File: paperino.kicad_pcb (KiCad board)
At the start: 2 copper layers, 25.4 x 22 mm, 21 parts, among them P1 CONN_01X06, P2 CONN_01X06, P3 CONN_01X06, P4 CONN_01X06, Q1 PMOS, Q2 NMOS, U1 BMA250E, X1 XF2M-2615-1A, X2 XF2B-4545-1A

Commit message: started layout
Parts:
- moved C3 1.25 mm to (140.7, 98.3)
- moved D1 1.19 mm to (140.3, 100.3), turned to 0 degrees
- moved C7 0.67 mm to (131.3, 95.4)
- moved C6 0.58 mm to (140.2, 95.3)
- moved C5 0.58 mm to (141.9, 95.3)
- moved C2 0.29 mm to (137.9, 97.7)
- moved C9 0.26 mm to (129.1, 95.4)
- moved C8 0.20 mm to (135.9, 94.3)
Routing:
- net /GDR_N: track 2.31 -> 22.1 mm, vias 0 -> 2
- net /INT1: track 0.00 -> 19.5 mm, vias 0 -> 1
- net /INT2: track 0.00 -> 19.1 mm, vias 0 -> 1
- net /VGH: track 4.98 -> 22.7 mm
- net /SPI_CLK: track 2.35 -> 19.7 mm, vias 0 -> 1
- net /SPI_MOSI: track 2.35 -> 18.3 mm, vias 0 -> 1
- net /SPI_CS2: track 0.00 -> 15.8 mm
- net /SPI_MISO: track 2.58 -> 18.3 mm, vias 0 -> 1
- net +3V3: track 12.3 -> 28.0 mm, vias 0 -> 2
- net /GDR_P: track 2.54 -> 14.7 mm, vias 0 -> 2
- net /VDD: track 11.3 -> 22.7 mm
- net /VGL: track 4.90 -> 15.8 mm
- net Net-(D1-Pad1): track 0.00 -> 9.41 mm
- net Net-(D2-Pad2): track 0.00 -> 7.93 mm
- net /VSH: track 4.81 -> 7.84 mm
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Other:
- net class Default: via_dia 0.6 -> 0.55; via_drill 0.4 -> 0.25
- rule via_min_drill: 0.3 -> 0.25
- rule via_min_size: 0.4 -> 0.55

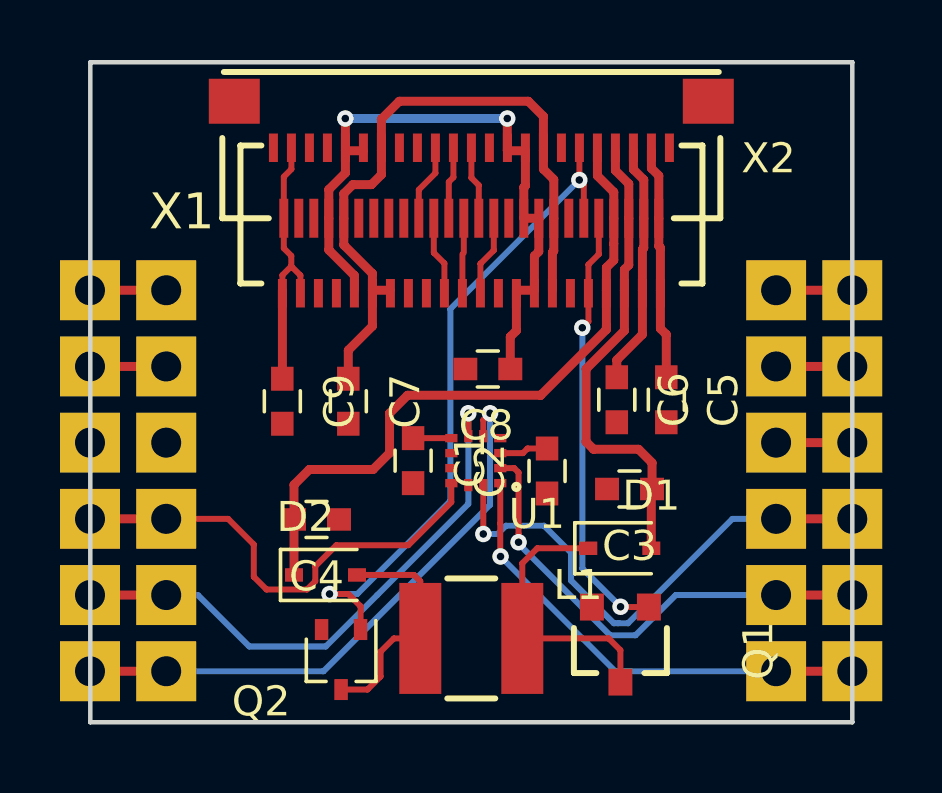
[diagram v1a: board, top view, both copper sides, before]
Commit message: finished preliminary layout
GND planes still missing
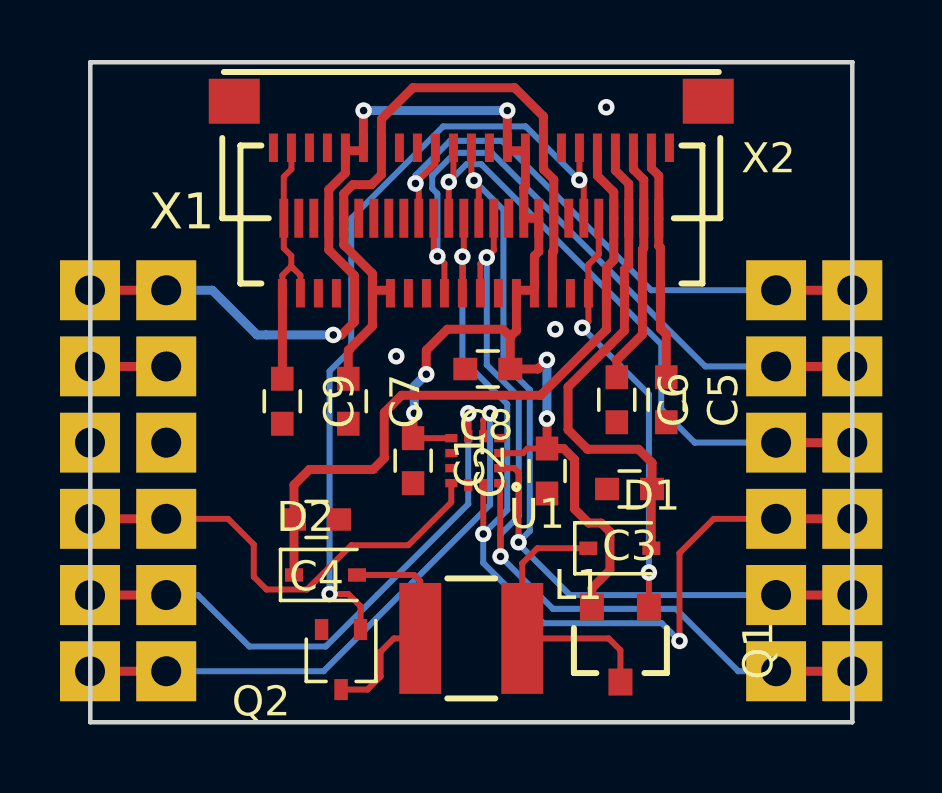
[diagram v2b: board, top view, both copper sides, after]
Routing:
- net +3V3: track 28.0 -> 53.6 mm, vias 2 -> 7
- net /~RST: track 5.09 -> 22.6 mm, vias 0 -> 1
- net /SPI_CS1: track 4.85 -> 21.1 mm, vias 0 -> 1
- net /~BUSY: track 5.02 -> 19.9 mm, vias 0 -> 1
- net /SPI_CLK: track 19.7 -> 32.0 mm, vias 1 -> 3
- net /SPI_MOSI: track 18.3 -> 30.2 mm, vias 1 -> 2
- net /SPI_MISO: track 18.3 -> 29.0 mm, vias 1 -> 2
- net /GDR_N: track 22.1 -> 26.7 mm
- net /VGL: track 15.8 -> 16.4 mm
- net /GDR_P: track 14.7 -> 14.1 mm
- net GND: vias 0 -> 3
- added copper zone on B.Cu, net GND
- added copper zone on F.Cu, net GND

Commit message: finished layout
GND pours and designator arrangemenent
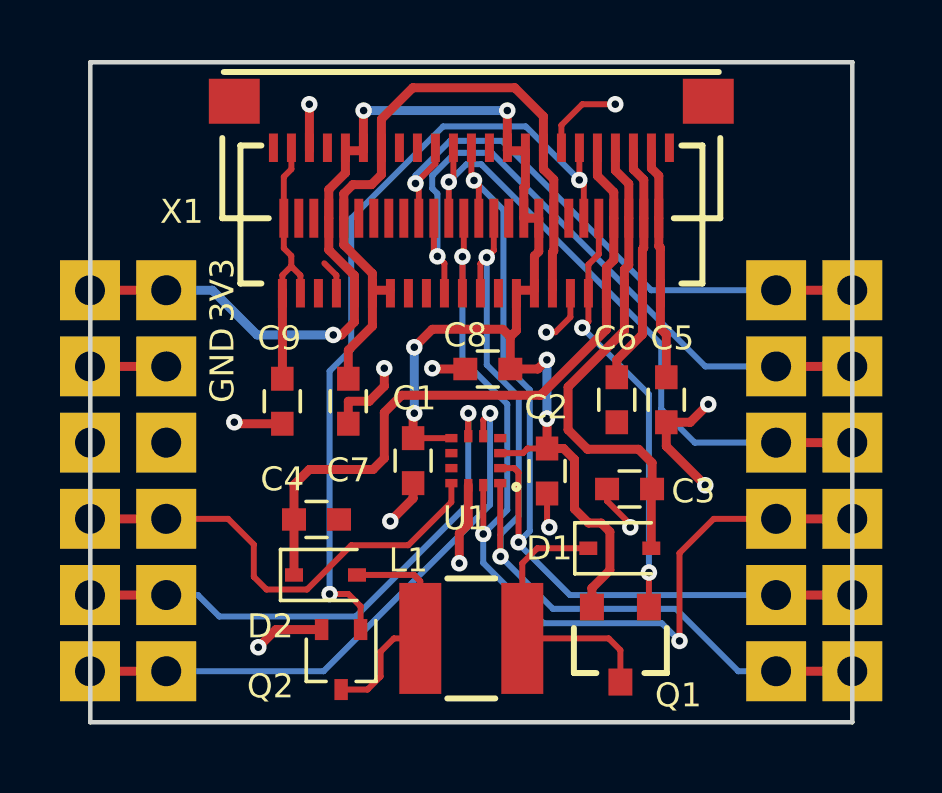
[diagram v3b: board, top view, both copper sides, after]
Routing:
- net GND: track 2.54 -> 29.2 mm, vias 3 -> 13
- net /INT2: track 19.1 -> 18.2 mm
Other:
- board text added: "3V3"
- board text added: "GND"

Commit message: fiducials added
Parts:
- added Fid1: Fiducial, Paperino:Fiducial, F.Cu at (124.0, 85.4)
- added Fid2: Fiducial, Paperino:Fiducial, F.Cu at (143.4, 104.9)
- added REF**: Fiducial, Fiducial, F.Cu at (0.00, 0.00)
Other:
- board text added: "CS2"
- board text added: "INT1"
- board text added: "INT2"
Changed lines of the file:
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@@
     (links 100)
     (no_connects 0)
-    (area 106.650001 84.024999 150.983334 108.395)
+    (area 122.624999 84.024999 148.175001 106.175001)
     (thickness 1.6)
-    (drawings 6)
+    (drawings 9)
     (tracks 350)
     (zones 0)
-    (modules 21)
+    (modules 24)
     (nets 38)
   )
@@
     (add_net "Net-(X2-Pad45)")
   )
+  (module Fiducial (layer F.Cu)
+    (at 0 0)
+    (fp_text reference REF** (at 0 2.54) (layer F.SilkS) hide
+      (effects (font (size 1 1) (thickness 0.15)))
+    )
+    (fp_text value Fiducial (at 0 -2.54) (layer F.Fab) hide
+      (effects (font (size 1 1) (thickness 0.15)))
+    )
+    (pad "" smd circle (at 0 0) (size 0.5 0.5) (layers F.Cu F.Mask)
+      (solder_mask_margin 0.5) (clearance 0.5))
+  )
   (module Paperino:XF2B-4545-31A (layer F.Cu)
     (at 142.004 87.05 180)
@@
     (at 140.37 103.51 270)
     (solder_mask_margin 0.07)
-    (fp_text reference Q1 (at 1.69 -1.93 540) (layer F.SilkS)
+    (fp_text reference Q1 (at 1.79 1.57 540) (layer F.SilkS)
       (effects (font (size 0.8 0.8) (thickness 0.15)))
     )
@@
     (pad 6 thru_hole rect (at 0 12.7) (size 2 2) (drill 1) (layers *.Cu *.Mask)
       (net 20 /INT1))
+  )
+  (module Paperino:Fiducial (layer F.Cu)
+    (at 124 85.4)
+    (fp_text reference Fid1 (at 0 -2.1) (layer F.SilkS) hide
+      (effects (font (size 1 1) (thickness 0.15)))
+    )
+    (fp_text value Fiducial (at 0 -2.54) (layer F.Fab) hide
+      (effects (font (size 1 1) (thickness 0.15)))
+    )
+    (pad "" smd circle (at 0 0) (size 0.5 0.5) (layers F.Cu F.Mask)
+      (solder_mask_margin 0.5) (clearance 0.5))
+  )
+  (module Paperino:Fiducial (layer F.Cu)
+    (at 143.4 104.9)
+    (fp_text reference Fid2 (at 0 2.1) (layer F.SilkS) hide
+      (effects (font (size 1 1) (thickness 0.15)))
+    )
+    (fp_text value Fiducial (at 0 -2.54) (layer F.Fab) hide
+      (effects (font (size 1 1) (thickness 0.15)))
+    )
+    (pad "" smd circle (at 0 0) (size 0.5 0.5) (layers F.Cu F.Mask)
+      (solder_mask_margin 0.5) (clearance 0.5))
+  )
+  (gr_text INT1 (at 127.1 104.6 90) (layer F.SilkS)
+    (effects (font (size 0.8 0.8) (thickness 0.15)))
+  )
+  (gr_text INT2 (at 127.1 101.9 90) (layer F.SilkS)
+    (effects (font (size 0.8 0.8) (thickness 0.15)))
+  )
+  (gr_text CS2 (at 127.1 99.3 90) (layer F.SilkS)
+    (effects (font (size 0.8 0.8) (thickness 0.15)))
   )
   (gr_text GND (at 127.1 94.2 90) (layer F.SilkS)
@@
     (min_thickness 0.254)
     (keepout (tracks not_allowed) (vias not_allowed) (copperpour not_allowed))
-    (fill (arc_segments 16) (thermal_gap 0.508) (thermal_bridge_width 0.508))
+    (fill yes (arc_segments 16) (thermal_gap 0.508) (thermal_bridge_width 0.508))
     (polygon
       (pts
@@
     (min_thickness 0.254)
     (keepout (tracks not_allowed) (vias not_allowed) (copperpour not_allowed))
-    (fill (arc_segments 16) (thermal_gap 0.508) (thermal_bridge_width 0.508))
+    (fill yes (arc_segments 16) (thermal_gap 0.508) (thermal_bridge_width 0.508))
     (polygon
       (pts
